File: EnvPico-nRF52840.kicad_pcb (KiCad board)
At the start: 2 copper layers, 21.2 x 57.7 mm, 48 parts, among them J3 2.54mm header 01x20, J4 2.54mm header 01x20, J5 Conn_01x03_Male, U1 LM3671MF 3.3, U2 BQ24072RGT, U3 nRF52840, Y1 32MHz 12pF

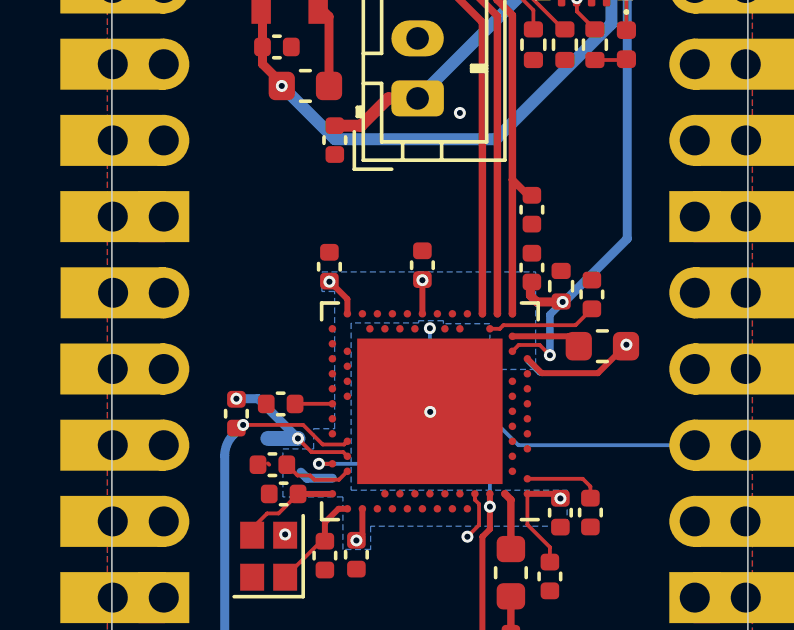
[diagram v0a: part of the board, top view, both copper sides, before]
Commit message: started adding some pins for GPIO
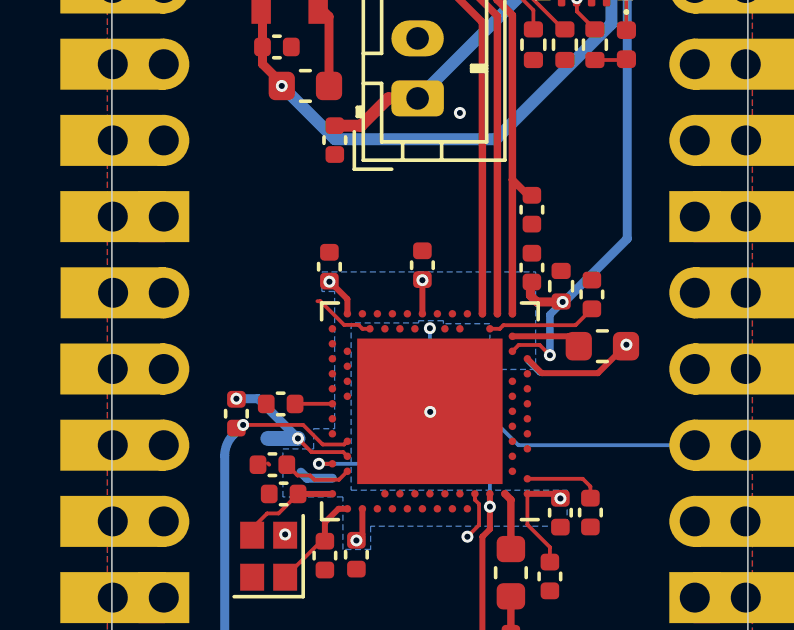
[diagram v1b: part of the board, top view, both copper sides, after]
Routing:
- net (no net): track 0.00 -> 2.13 mm
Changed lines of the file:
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@@
     (style (thickness 0.15) (arrow_length 1.27) (text_position_mode 0) (extension_height 0.58642) (extension_offset 0) keep_text_aligned)
   )
+  (segment (start 101.39 80.245) (end 101.26 80.115) (width 0.127) (layer "F.Cu") (net 0))
+  (segment (start 101.26 80.115) (end 100.78 80.115) (width 0.127) (layer "F.Cu") (net 0))
+  (segment (start 101.64 80.245) (end 101.39 80.245) (width 0.127) (layer "F.Cu") (net 0))
+  (segment (start 100.78 80.115) (end 99.99 79.325) (width 0.127) (layer "F.Cu") (net 0))
+  (segment (start 99.99 79.325) (end 99.89 79.325) (width 0.127) (layer "F.Cu") (net 0))
   (segment (start 105.14 85.946268) (end 105.14 85.745) (width 0.127) (layer "F.Cu") (net 1))
   (segment (start 104.89 87.175) (end 105.278011 86.786989) (width 0.127) (layer "F.Cu") (net 1))

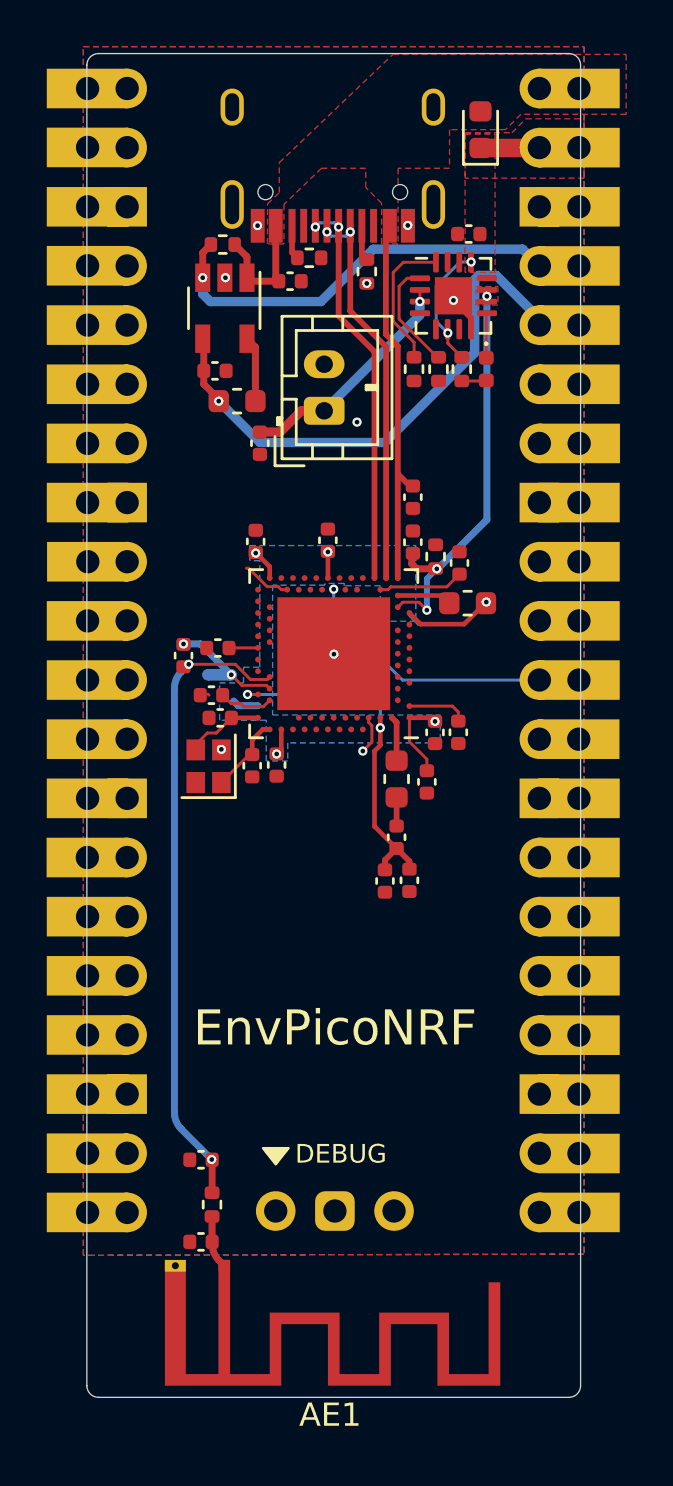
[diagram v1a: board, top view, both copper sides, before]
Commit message: made sure all vias are correctly placed and sized.
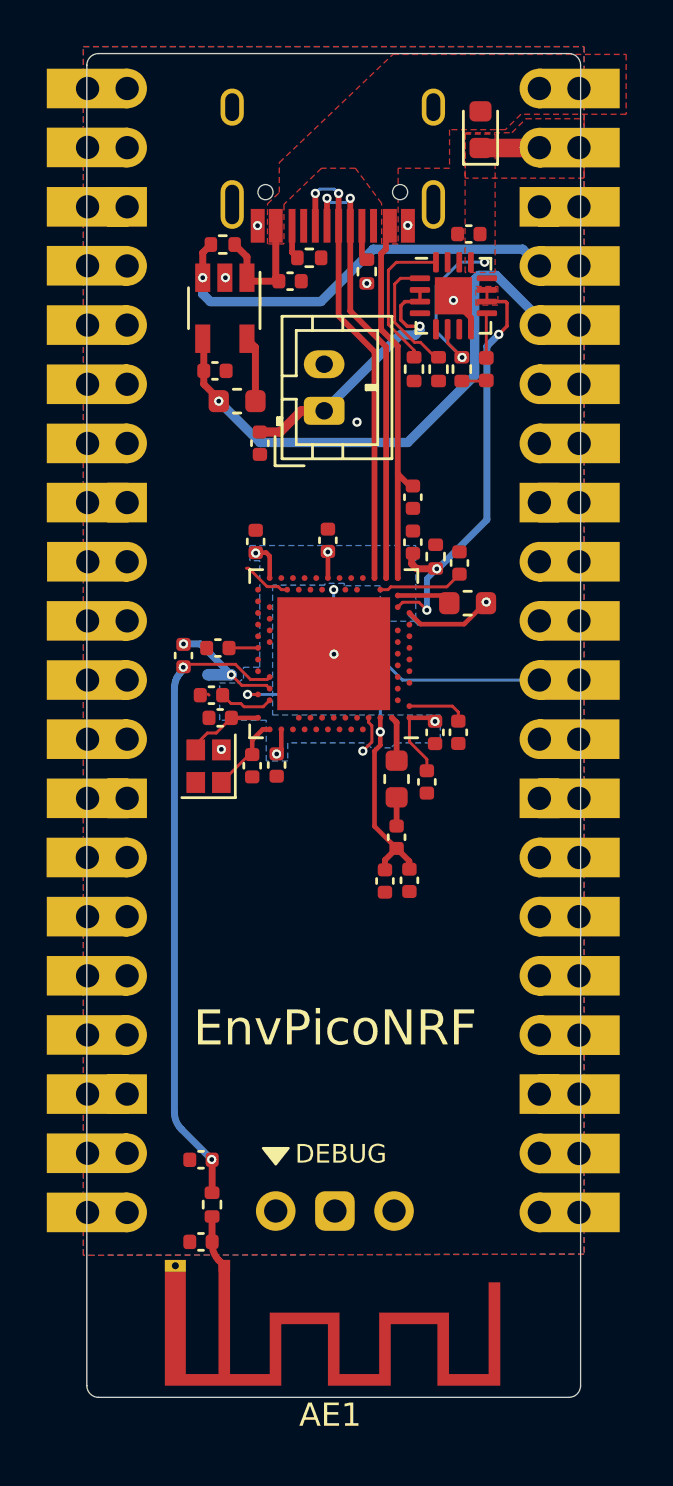
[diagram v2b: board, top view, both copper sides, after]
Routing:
- net USB_D+: track 16.9 -> 19.7 mm
- net USB_D-: track 18.2 -> 20.5 mm
- net GND: track 3.46 -> 5.59 mm
- net (no net): track 2.13 -> 0.00 mm
- net VSYS: track 7.98 -> 9.85 mm
- net Net-(BT1-Pad1): track 10.0 -> 11.8 mm
- net VDDH: track 18.2 -> 19.2 mm
- net VDD_NRF: track 16.2 -> 15.4 mm
- net 3.3VO: track 23.3 -> 23.9 mm
- net Net-(R12-Pad2): track 4.81 -> 5.34 mm

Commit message: connected all 26 GPIOs among other things.
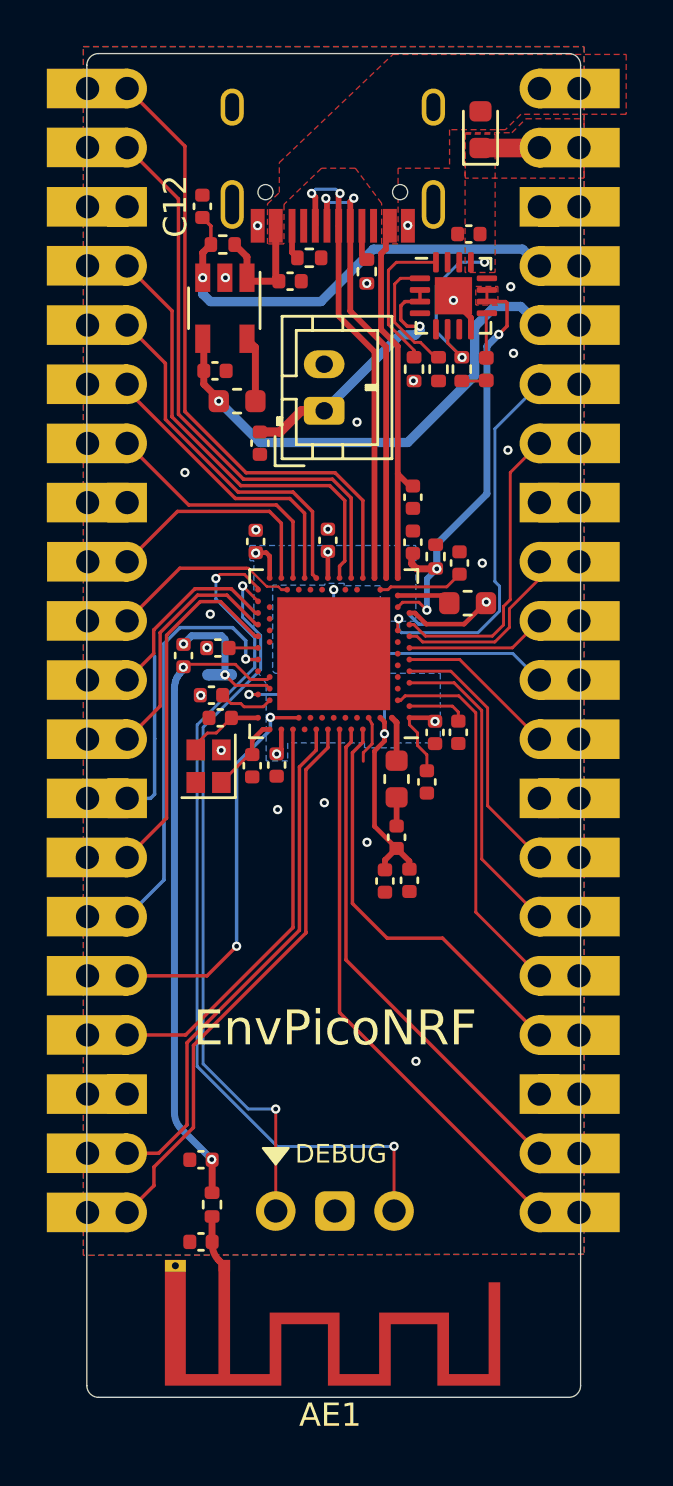
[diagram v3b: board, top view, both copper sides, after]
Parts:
- added C12: 0.1uf 0402, Capacitor_SMD:C_0402_1005Metric, F.Cu at (98.0, 63.8)
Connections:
- J3 pad 1: unconnected-(J3-Pad1) -> GPIO15
- J3 pad 10: unconnected-(J3-Pad10) -> GPIO8
- J3 pad 11: unconnected-(J3-Pad11) -> GPIO7
- J3 pad 12: unconnected-(J3-Pad12) -> GPIO6
- J3 pad 14: unconnected-(J3-Pad14) -> GPIO5
- J3 pad 15: unconnected-(J3-Pad15) -> GPIO4
- J3 pad 16: unconnected-(J3-Pad16) -> GPIO3
- J3 pad 17: unconnected-(J3-Pad17) -> GPIO2
- J3 pad 19: unconnected-(J3-Pad19) -> GPIO1
- J3 pad 2: unconnected-(J3-Pad2) -> GPIO14
- J3 pad 20: unconnected-(J3-Pad20) -> GPIO0
- J3 pad 4: unconnected-(J3-Pad4) -> GPIO13
- J3 pad 5: unconnected-(J3-Pad5) -> GPIO12
- J3 pad 6: unconnected-(J3-Pad6) -> GPIO11
- J3 pad 7: unconnected-(J3-Pad7) -> GPIO10
- J3 pad 9: unconnected-(J3-Pad9) -> GPIO9
- J4 pad 10: unconnected-(J4-Pad10) -> GPIO23
- J4 pad 12: unconnected-(J4-Pad12) -> GPIO22
- J4 pad 14: unconnected-(J4-Pad14) -> GPIO21
- J4 pad 15: unconnected-(J4-Pad15) -> GPIO20
- J4 pad 16: unconnected-(J4-Pad16) -> GPIO19
- J4 pad 17: unconnected-(J4-Pad17) -> GPIO18
- J4 pad 19: unconnected-(J4-Pad19) -> GPIO17
- J4 pad 20: unconnected-(J4-Pad20) -> GPIO16
- J4 pad 6: unconnected-(J4-Pad6) -> GPIO26
- J4 pad 7: unconnected-(J4-Pad7) -> GPIO25
- J4 pad 9: unconnected-(J4-Pad9) -> GPIO24
- U2 pad 12: (no net) -> unconnected-(U2-Pad12)
- U2 pad 14: (no net) -> unconnected-(U2-Pad14)
- U2 pad 7: (no net) -> unconnected-(U2-Pad7)
- U3 pad A10: (no net) -> GPIO17
- U3 pad A12: (no net) -> GPIO16
- U3 pad A14: (no net) -> GPIO15
- U3 pad A16: (no net) -> GPIO14
- U3 pad A18: (no net) -> unconnected-(U3-PadA18)
- U3 pad A20: (no net) -> GPIO13
- U3 pad A8: (no net) -> GPIO18
- U3 pad AC11: (no net) -> unconnected-(U3-PadAC11)
- U3 pad AC15: (no net) -> unconnected-(U3-PadAC15)
- U3 pad AC17: (no net) -> unconnected-(U3-PadAC17)
- U3 pad AC19: (no net) -> unconnected-(U3-PadAC19)
- U3 pad AC21: (no net) -> GPIO7
- U3 pad AC9: (no net) -> unconnected-(U3-PadAC9)
- U3 pad AD10: (no net) -> GPIO1
- U3 pad AD12: (no net) -> GPIO2
- U3 pad AD16: (no net) -> GPIO3
- U3 pad AD18: (no net) -> GPIO4
- U3 pad AD20: (no net) -> GPIO5
- U3 pad AD22: (no net) -> GPIO6
- U3 pad AD8: (no net) -> GPIO0
- U3 pad B11: (no net) -> unconnected-(U3-PadB11)
- U3 pad B13: (no net) -> unconnected-(U3-PadB13)
- U3 pad B15: (no net) -> unconnected-(U3-PadB15)
- U3 pad B17: (no net) -> unconnected-(U3-PadB17)
- U3 pad B19: (no net) -> GPIO12
- U3 pad B9: (no net) -> unconnected-(U3-PadB9)
- U3 pad D2: (no net) -> GPIO19
- U3 pad F2: (no net) -> unconnected-(U3-PadF2)
- U3 pad G1: (no net) -> GPIO20
- U3 pad H2: (no net) -> unconnected-(U3-PadH2)
- U3 pad J1: (no net) -> GPIO21
- U3 pad J24: (no net) -> unconnected-(U3-PadJ24)
- U3 pad K2: (no net) -> unconnected-(U3-PadK2)
- U3 pad L1: (no net) -> GPIO22
- U3 pad L24: (no net) -> GPIO11
- U3 pad M2: (no net) -> unconnected-(U3-PadM2)
- U3 pad N1: (no net) -> GPIO23
- U3 pad P2: (no net) -> unconnected-(U3-PadP2)
- U3 pad P23: (no net) -> unconnected-(U3-PadP23)
- U3 pad R1: (no net) -> GPIO24
- U3 pad R24: (no net) -> GPIO10
- U3 pad T2: (no net) -> GPIO26
- U3 pad T23: (no net) -> unconnected-(U3-PadT23)
- U3 pad U1: (no net) -> GPIO25
- U3 pad U24: (no net) -> GPIO9
- U3 pad V23: (no net) -> unconnected-(U3-PadV23)
- U3 pad W24: (no net) -> GPIO8
- U3 pad Y23: (no net) -> unconnected-(U3-PadY23)
- e1 pad 3: (no net) -> unconnected-(e1-Pad3)
- e1 pad 9: (no net) -> unconnected-(e1-Pad9)
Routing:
- net /SWD: track 0.00 -> 37.5 mm, vias 0 -> 2
- net /SWCLK: track 0.00 -> 31.1 mm, vias 0 -> 2
- net GPIO0: track 0.00 -> 27.4 mm
- net GPIO1: track 0.00 -> 24.7 mm
- net GPIO15: track 0.00 -> 24.3 mm
- net GPIO16: track 0.00 -> 24.3 mm
- net GPIO14: track 0.00 -> 22.4 mm
- net GPIO17: track 0.00 -> 21.7 mm
- net GPIO2: track 0.00 -> 19.6 mm
- net GPIO18: track 0.00 -> 18.0 mm
- net GPIO11: track 0.00 -> 17.7 mm, vias 0 -> 1
- net GPIO13: track 0.00 -> 17.5 mm
- net GPIO12: track 0.00 -> 16.9 mm, vias 0 -> 2
- net GPIO26: track 0.00 -> 16.4 mm, vias 0 -> 1
- net GPIO19: track 0.00 -> 16.2 mm
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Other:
- board text removed: "There is no treasure here"

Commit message: changed 2012 crystal for a 3225 size due to part availability. + went through and did a general clean up and correction per DRC.
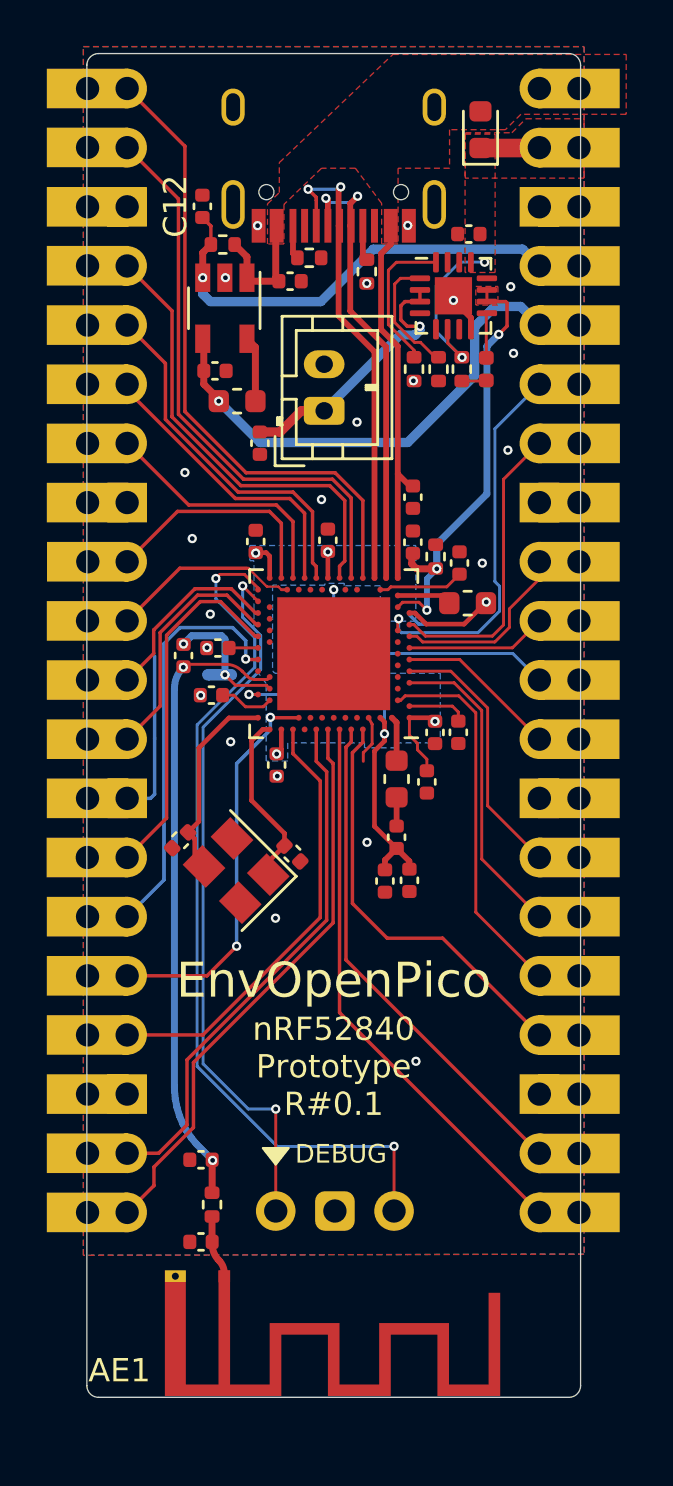
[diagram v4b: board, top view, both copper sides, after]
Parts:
- Y1: footprint Crystal:Crystal_SMD_2016-4Pin_2.0x1.6mm -> Crystal:Crystal_SMD_3225-4Pin_3.2x2.5mm
- moved C10 5.53 mm to (97.0, 91.0), turned to 45 degrees
- moved Y1 4.63 mm to (99.5, 92.3), turned to 135 degrees
- moved C11 4.15 mm to (101.9, 91.6), turned to 135 degrees
- moved AE1 0.45 mm to (98.9, 109.7)
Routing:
- net Net-(C10-Pad2): track 3.38 -> 8.64 mm
- net Net-(C11-Pad2): track 3.59 -> 7.61 mm
- net GPIO13: track 17.5 -> 18.9 mm
- net USB_D-: track 20.8 -> 19.9 mm
- net USB_D+: track 20.0 -> 20.6 mm
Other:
- board text added: "EnvOpenPico"
- board text added: "nRF52840 Prototype R#0.1"
- board text removed: "EnvPicoNRF"
